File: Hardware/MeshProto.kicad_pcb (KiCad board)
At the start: 2 copper layers, 30.2 x 31.6 mm, 27 parts, among them P1 CONN_1, P10 CONN_1, P11 CONN_1, P12 CONN_1, P13 CONN_1, P14 CONN_1, P15 CONN_1, P16 CONN_1, P17 CONN_1, P18 CONN_1, P19 CONN_1, P2 CONN_1, P20 CONN_1, P3 CONN_1, P4 CONN_1, P5 CONN_1, P6 CONN_1, P7 CONN_1, P8 CONN_1, P9 CONN_1, U1 XBEE

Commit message: v02
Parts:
- added P21: CONN_1, _MP_1Pin, F.Cu at (147.3, 114.3)
- added P22: CONN_1, _MP_1Pin, F.Cu at (152.4, 121.9)
- added P23: CONN_1, _MP_1Pin, F.Cu at (154.9, 121.9)
- added P24: CONN_1, _MP_1Pin, F.Cu at (149.9, 119.4)
- added P25: CONN_1, _MP_1Pin, F.Cu at (147.3, 119.4)
- added P26: CONN_1, _MP_1Pin, F.Cu at (144.8, 119.4)
- added P27: CONN_1, _MP_1Pin, F.Cu at (142.2, 119.4)
- added P28: CONN_1, _MP_1Pin, F.Cu at (154.9, 116.8)
- added P29: CONN_1, _MP_1Pin, F.Cu at (147.3, 116.8)
- added P30: CONN_1, _MP_1Pin, F.Cu at (154.9, 111.8)
- added P31: CONN_1, _MP_1Pin, F.Cu at (142.2, 111.8)
- added P32: CONN_1, _MP_1Pin, F.Cu at (147.3, 111.8)
- added P33: CONN_1, _MP_1Pin, F.Cu at (144.8, 111.8)
- added P34: CONN_1, _MP_1Pin, F.Cu at (147.3, 109.2)
- added P35: CONN_1, _MP_1Pin, F.Cu at (144.8, 109.2)
- added P36: CONN_1, _MP_1Pin, F.Cu at (144.8, 116.8)
- added P37: CONN_1, _MP_1Pin, F.Cu at (152.4, 111.8)
- added P38: CONN_1, _MP_1Pin, F.Cu at (149.9, 111.8)
- added P39: CONN_1, _MP_1Pin, F.Cu at (152.4, 116.8)
- added P40: CONN_1, _MP_1Pin, F.Cu at (142.2, 109.2)
- added P41: CONN_1, _MP_1Pin, F.Cu at (149.9, 116.8)
- added P42: CONN_1, _MP_1Pin, F.Cu at (142.2, 116.8)
- added P43: CONN_1, _MP_1Pin, F.Cu at (154.9, 114.3)
- added P44: CONN_1, _MP_1Pin, F.Cu at (149.9, 109.2)
- added P45: CONN_1, _MP_1Pin, F.Cu at (149.9, 114.3)
- added P46: CONN_1, _MP_1Pin, F.Cu at (142.2, 114.3)
- added P47: CONN_1, _MP_1Pin, F.Cu at (152.4, 114.3)
- added P48: CONN_1, _MP_1Pin, F.Cu at (144.8, 114.3)
- added P49: CONN_1, _MP_1Pin, F.Cu at (154.9, 119.4)
- added P50: CONN_1, _MP_1Pin, F.Cu at (152.4, 124.5)
- added P51: CONN_1, _MP_1Pin, F.Cu at (149.9, 124.5)
- added P52: CONN_1, _MP_1Pin, F.Cu at (149.9, 121.9)
- added P53: CONN_1, _MP_1Pin, F.Cu at (147.3, 121.9)
- added P54: CONN_1, _MP_1Pin, F.Cu at (147.3, 124.5)
- added P55: CONN_1, _MP_1Pin, F.Cu at (144.8, 121.9)
- added P56: CONN_1, _MP_1Pin, F.Cu at (142.2, 121.9)
- added P57: CONN_1, _MP_1Pin, F.Cu at (142.2, 124.5)
- added P58: CONN_1, _MP_1Pin, F.Cu at (144.8, 124.5)
- added P59: CONN_1, _MP_1Pin, F.Cu at (154.9, 124.5)
- added P60: CONN_1, _MP_1Pin, F.Cu at (152.4, 119.4)
- added P61: CONN_1, _MP_1Pin, F.Cu at (144.8, 101.6)
- added P62: CONN_1, _MP_1Pin, F.Cu at (152.4, 106.7)
- added P63: CONN_1, _MP_1Pin, F.Cu at (147.3, 106.7)
- added P64: CONN_1, _MP_1Pin, F.Cu at (149.9, 106.7)
- added P65: CONN_1, _MP_1Pin, F.Cu at (149.9, 101.6)
- added P66: CONN_1, _MP_1Pin, F.Cu at (154.9, 106.7)
- added P67: CONN_1, _MP_1Pin, F.Cu at (154.9, 104.1)
- added P68: CONN_1, _MP_1Pin, F.Cu at (144.8, 106.7)
- added P69: CONN_1, _MP_1Pin, F.Cu at (152.4, 104.1)
- added P70: CONN_1, _MP_1Pin, F.Cu at (149.9, 104.1)
- added P71: CONN_1, _MP_1Pin, F.Cu at (152.4, 109.2)
- added P72: CONN_1, _MP_1Pin, F.Cu at (154.9, 101.6)
- added P73: CONN_1, _MP_1Pin, F.Cu at (147.3, 104.1)
- added P74: CONN_1, _MP_1Pin, F.Cu at (154.9, 109.2)
- added P75: CONN_1, _MP_1Pin, F.Cu at (142.2, 106.7)
- added P76: CONN_1, _MP_1Pin, F.Cu at (142.2, 104.1)
- added P77: CONN_1, _MP_1Pin, F.Cu at (142.2, 101.6)
- added P78: CONN_1, _MP_1Pin, F.Cu at (147.3, 101.6)
- added P79: CONN_1, _MP_1Pin, F.Cu at (152.4, 101.6)
- added P80: CONN_1, _MP_1Pin, F.Cu at (144.8, 104.1)
- moved P15 9.92 mm to (157.5, 111.8)
- moved P3 8.89 mm to (139.7, 106.7)
- moved P8 8.89 mm to (139.7, 119.4)
- moved P16 6.35 mm to (157.5, 114.3)
- moved P11 5.81 mm to (157.5, 101.6)
- moved P1 5.24 mm to (139.7, 101.6)
- moved P2 5.24 mm to (139.7, 104.1)
- moved P5 5.24 mm to (139.7, 111.8)
- moved P20 5.24 mm to (157.5, 124.5)
- moved P4 5.08 mm to (139.7, 109.2)
- moved P7 5.08 mm to (139.7, 116.8)
- moved P12 4.58 mm to (157.5, 104.1)
- moved P17 4.58 mm to (157.5, 116.8)
- moved P18 3.59 mm to (157.5, 119.4)
- moved P10 2.84 mm to (139.7, 124.5)
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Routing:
- net N-0000097: track 15.0 -> 0.00 mm
- net N-0000088: track 12.1 -> 0.00 mm
- net N-0000075: track 11.2 -> 0.00 mm
- net N-0000098: track 8.66 -> 0.00 mm
- net BAT+: track 8.16 -> 0.00 mm
- net N-0000089: track 8.02 -> 0.00 mm
- net N-0000087: track 7.94 -> 0.00 mm
- net N-0000092: track 7.35 -> 0.00 mm
- net N-0000090: track 7.29 -> 0.00 mm
- net N-0000094: track 7.24 -> 0.00 mm
- net N-0000085: track 7.18 -> 0.00 mm
- net N-0000099: track 6.49 -> 0.00 mm
- net N-0000096: track 6.11 -> 0.00 mm
- net N-00000100: track 5.46 -> 0.00 mm
- net N-0000095: track 4.95 -> 0.00 mm
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
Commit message: Layout Almost Complete
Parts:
- added P81: CONN_1, _MP_1Pin, F.Cu at (134.6, 106.7)
- added P82: CONN_1, _MP_1Pin, F.Cu at (134.6, 109.2)
- added P83: CONN_1, _MP_1Pin, F.Cu at (142.2, 100.1)
- added P84: CONN_1, _MP_1Pin, F.Cu at (149.9, 100.1)
- added P85: CONN_1, _MP_1Pin, F.Cu at (152.4, 100.1)
- added P86: CONN_1, _MP_1Pin, F.Cu at (154.9, 100.1)
- added P87: CONN_1, _MP_1Pin, F.Cu at (144.8, 100.1)
- added P88: CONN_1, _MP_1Pin, F.Cu at (147.3, 100.1)
- added P89: CONN_1, _MP_1Pin, F.Cu at (154.9, 128.0)
- added P90: CONN_1, _MP_1Pin, F.Cu at (144.8, 128.0)
- added P91: CONN_1, _MP_1Pin, F.Cu at (142.2, 128.0)
- added P92: CONN_1, _MP_1Pin, F.Cu at (152.4, 128.0)
- added P93: CONN_1, _MP_1Pin, F.Cu at (149.9, 128.0)
- added P94: CONN_1, _MP_1Pin, F.Cu at (147.3, 128.0)
- added SW1: SPST, _MT_TC007-TactileSwitch, F.Cu at (134.7, 116.8)
- moved P1 1.02 mm to (139.7, 102.6)
- moved P10 1.02 mm to (139.7, 125.5)
- moved P11 1.02 mm to (157.5, 102.6)
- moved P12 1.02 mm to (157.5, 105.2)
- moved P14 1.02 mm to (157.5, 110.2)
- moved P16 1.02 mm to (157.5, 115.3)
- moved P18 1.02 mm to (157.5, 120.4)
- moved P19 1.02 mm to (157.5, 122.9)
- moved P2 1.02 mm to (139.7, 105.2)
- moved P20 1.02 mm to (157.5, 125.5)
- moved P21 1.02 mm to (147.3, 115.3)
- moved P22 1.02 mm to (152.4, 122.9)
- moved P23 1.02 mm to (154.9, 122.9)
- moved P24 1.02 mm to (149.9, 120.4)
- moved P25 1.02 mm to (147.3, 120.4)
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
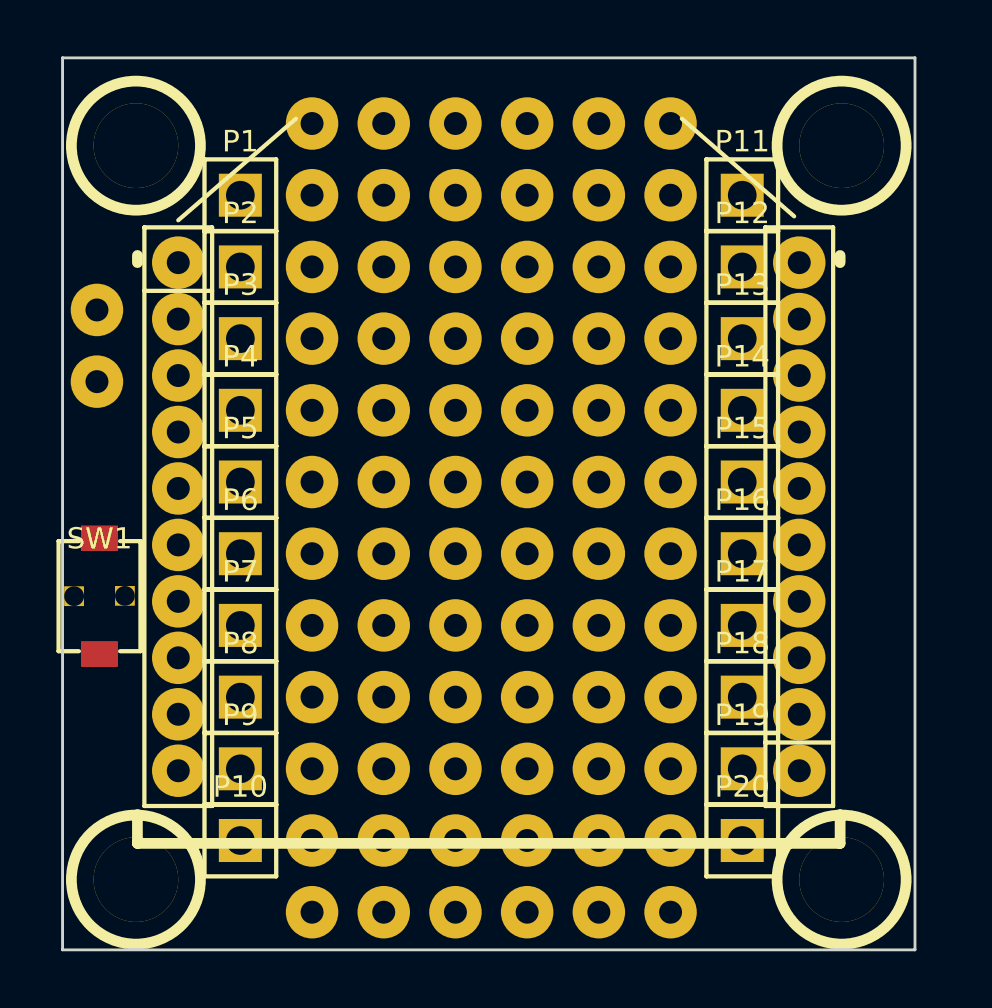
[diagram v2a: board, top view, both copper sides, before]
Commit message: Added labels
Added GND and BAT+ labels to silkscreen.
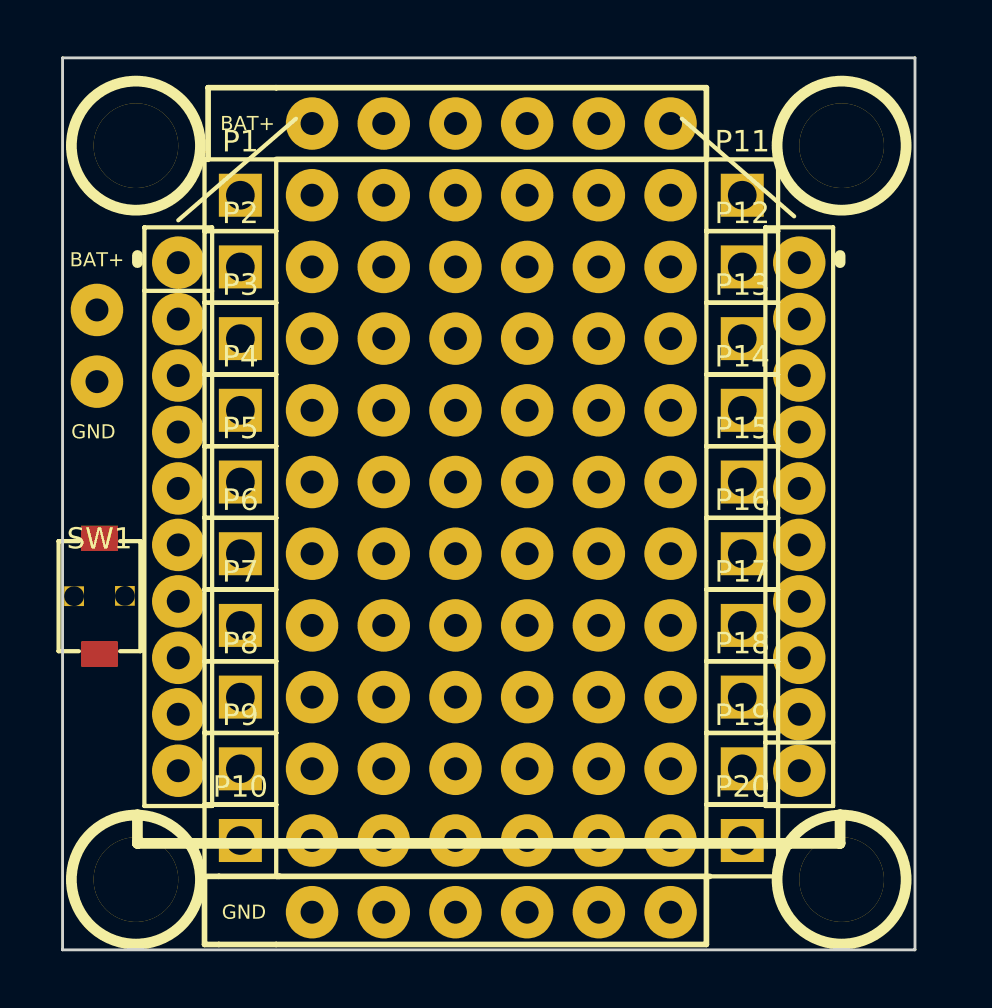
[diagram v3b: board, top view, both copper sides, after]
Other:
- board text added: "BAT+"
- board text added: "GND"
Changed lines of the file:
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@@
     (area 130.555134 96.9738 167.000422 130.4922)
     (thickness 1.6)
-    (drawings 4)
+    (drawings 21)
     (tracks 0)
     (zones 0)
@@
     )
   )
+  (gr_text GND (at 134.493 110.998) (layer F.SilkS)
+    (effects (font (size 0.5 0.5) (thickness 0.1)))
+  )
+  (gr_text BAT+ (at 134.62 104.902) (layer F.SilkS)
+    (effects (font (size 0.5 0.5) (thickness 0.1)))
+  )
+  (gr_text BAT+ (at 139.954 100.076) (layer F.SilkS)
+    (effects (font (size 0.5 0.5) (thickness 0.1)))
+  )
+  (gr_line (start 140.97 98.806) (end 138.557 98.806) (angle 90) (layer F.SilkS) (width 0.2))
+  (gr_line (start 138.557 101.346) (end 138.557 98.806) (angle 90) (layer F.SilkS) (width 0.2))
+  (gr_line (start 138.43 129.159) (end 138.938 129.159) (angle 90) (layer F.SilkS) (width 0.2))
+  (gr_line (start 138.43 126.746) (end 138.43 129.159) (angle 90) (layer F.SilkS) (width 0.2))
+  (gr_line (start 138.938 126.746) (end 138.43 126.746) (angle 90) (layer F.SilkS) (width 0.2))
+  (gr_line (start 138.938 126.746) (end 141.097 126.746) (angle 90) (layer F.SilkS) (width 0.2))
+  (gr_line (start 140.97 129.159) (end 138.938 129.159) (angle 90) (layer F.SilkS) (width 0.2))
+  (gr_text GND (at 139.827 128.016) (layer F.SilkS)
+    (effects (font (size 0.5 0.5) (thickness 0.1)))
+  )
+  (gr_line (start 156.21 129.159) (end 140.97 129.159) (angle 90) (layer F.SilkS) (width 0.2))
+  (gr_line (start 156.21 126.746) (end 156.21 129.159) (angle 90) (layer F.SilkS) (width 0.2))
+  (gr_line (start 140.97 126.746) (end 156.337 126.746) (angle 90) (layer F.SilkS) (width 0.2))
+  (gr_line (start 156.21 98.806) (end 156.21 101.346) (angle 90) (layer F.SilkS) (width 0.2))
+  (gr_line (start 140.97 98.806) (end 156.21 98.806) (angle 90) (layer F.SilkS) (width 0.2))
+  (gr_line (start 156.083 101.346) (end 140.97 101.346) (angle 90) (layer F.SilkS) (width 0.2))
   (gr_line (start 163.6 97.75) (end 163.6 129.35) (angle 90) (layer Edge.Cuts) (width 0.1))
   (gr_line (start 133.4 97.75) (end 163.6 97.75) (angle 90) (layer Edge.Cuts) (width 0.1))

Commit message: Totally Wired Up
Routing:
- net GND: track 0.00 -> 35.9 mm
- net BAT+: track 0.00 -> 23.2 mm
- net N-0000052: track 0.00 -> 5.82 mm
- net N-0000072: track 0.00 -> 3.31 mm
- net N-0000063: track 0.00 -> 3.22 mm
- net N-0000062: track 0.00 -> 3.00 mm
- net N-0000058: track 0.00 -> 2.97 mm
- net N-0000071: track 0.00 -> 2.82 mm
- net N-0000064: track 0.00 -> 2.79 mm
- net N-0000059: track 0.00 -> 2.78 mm
- net N-0000057: track 0.00 -> 2.74 mm
- net N-0000070: track 0.00 -> 2.60 mm
- net N-0000065: track 0.00 -> 2.56 mm
- net N-0000054: track 0.00 -> 2.55 mm
- net N-0000056: track 0.00 -> 2.52 mm
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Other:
- board text added: "3v3"
- board text added: "MeshProto v1.0 © David Chanter, Bob Powers, Andy Gelme"
- board text added: "This Way Up"
- board text added: "meshthing.com"
- board text added: "↑"
- board text removed: "BAT+"

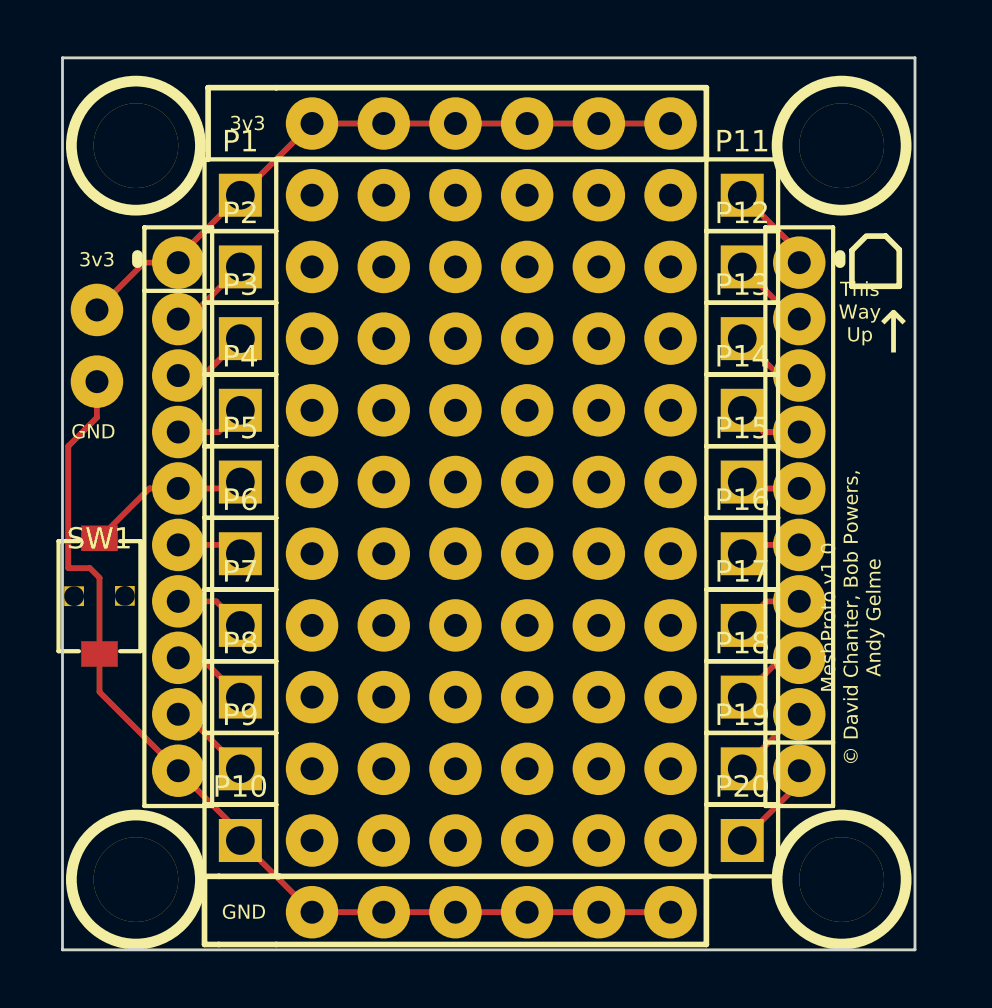
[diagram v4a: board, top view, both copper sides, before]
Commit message: Increased track width. Routed GND on back to move it away from the board edge.
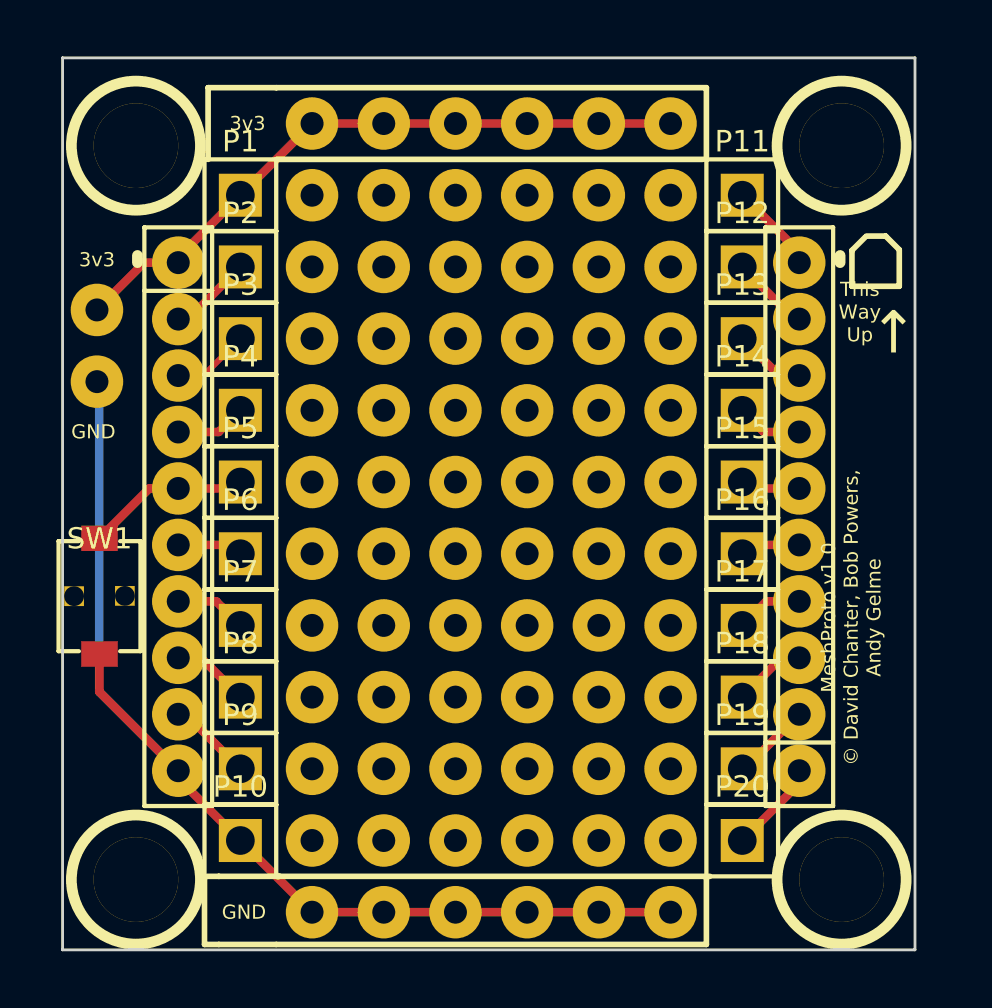
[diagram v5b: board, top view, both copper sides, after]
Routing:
- net BAT+: track 23.2 -> 42.6 mm
- net GND: track 35.9 -> 52.6 mm
- net N-0000052: track 5.82 -> 8.81 mm
- net N-0000062: track 3.00 -> 5.73 mm
- net N-0000064: track 2.79 -> 5.40 mm
- net N-0000070: track 2.60 -> 4.57 mm
- net N-0000059: track 2.78 -> 4.75 mm
- net N-0000067: track 2.11 -> 3.91 mm
- net N-0000056: track 2.52 -> 3.95 mm
- net N-0000054: track 2.55 -> 3.90 mm
- net N-0000069: track 2.37 -> 3.54 mm
- net N-0000066: track 2.34 -> 3.42 mm
- net N-0000065: track 2.56 -> 3.27 mm

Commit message: Added OSHW logo, cleaned up libs.
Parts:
- added G***: LOGO, OSHWLogo:LOGO, F.Cu at (157.5, 100.1)
